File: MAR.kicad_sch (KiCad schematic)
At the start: 30 parts, among them J1 Conn_02x10_Odd_Even, J3 Conn_01x08_Pin, Q1 DMN3404, U1 74HC173, U3 74HC173

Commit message: increased resistor values for leds
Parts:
- R10, R11, R4, R5, R6, R7, R8, R9: value 200 -> 330; LCSC C25087 -> C25104
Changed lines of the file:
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@@
       (effects (font (size 1.27 1.27)) (justify left) hide)
     )
-    (property "Value" "200" (at 229.87 49.53 0)
+    (property "Value" "330" (at 229.87 49.53 0)
       (effects (font (size 1.27 1.27)) (justify left) hide)
     )
@@
       (effects (font (size 1.27 1.27)) hide)
     )
-    (property "LCSC" "C25087" (at 228.6 51.435 0)
+    (property "LCSC" "C25104" (at 228.6 51.435 0)
       (effects (font (size 1.27 1.27)) hide)
     )
@@
       (effects (font (size 1.27 1.27)) (justify left) hide)
     )
-    (property "Value" "200" (at 240.665 60.96 0)
+    (property "Value" "330" (at 240.665 60.96 0)
       (effects (font (size 1.27 1.27)) (justify left) hide)
     )
@@
       (effects (font (size 1.27 1.27)) hide)
     )
-    (property "LCSC" "C25087" (at 239.395 62.865 0)
+    (property "LCSC" "C25104" (at 239.395 62.865 0)
       (effects (font (size 1.27 1.27)) hide)
     )
@@
       (effects (font (size 1.27 1.27)) (justify left) hide)
     )
-    (property "Value" "200" (at 215.265 31.115 0)
+    (property "Value" "330" (at 215.265 31.115 0)
       (effects (font (size 1.27 1.27)) (justify left) hide)
     )
@@
       (effects (font (size 1.27 1.27)) hide)
     )
-    (property "LCSC" "C25087" (at 213.995 33.02 0)
+    (property "LCSC" "C25104" (at 213.995 33.02 0)
       (effects (font (size 1.27 1.27)) hide)
     )
@@
       (effects (font (size 1.27 1.27)) (justify left) hide)
     )
-    (property "Value" "200" (at 224.79 43.815 0)
+    (property "Value" "330" (at 224.79 43.815 0)
       (effects (font (size 1.27 1.27)) (justify left) hide)
     )
@@
       (effects (font (size 1.27 1.27)) hide)
     )
-    (property "LCSC" "C25087" (at 223.52 45.72 0)
+    (property "LCSC" "C25104" (at 223.52 45.72 0)
       (effects (font (size 1.27 1.27)) hide)
     )
@@
       (effects (font (size 1.27 1.27)) (justify left) hide)
     )
-    (property "Value" "200" (at 211.455 24.13 0)
+    (property "Value" "330" (at 211.455 24.13 0)
       (effects (font (size 1.27 1.27)) (justify left) hide)
     )
@@
       (effects (font (size 1.27 1.27)) hide)
     )
-    (property "LCSC" "C25087" (at 210.185 26.035 0)
+    (property "LCSC" "C25104" (at 210.185 26.035 0)
       (effects (font (size 1.27 1.27)) hide)
     )
@@
       (effects (font (size 1.27 1.27)) (justify left) hide)
     )
-    (property "Value" "200" (at 219.71 37.465 0)
+    (property "Value" "330" (at 219.71 37.465 0)
       (effects (font (size 1.27 1.27)) (justify left) hide)
     )
@@
       (effects (font (size 1.27 1.27)) hide)
     )
-    (property "LCSC" "C25087" (at 218.44 39.37 0)
+    (property "LCSC" "C25104" (at 218.44 39.37 0)
       (effects (font (size 1.27 1.27)) hide)
     )
@@
       (effects (font (size 1.27 1.27)) (justify left) hide)
     )
-    (property "Value" "200" (at 235.585 55.245 0)
+    (property "Value" "330" (at 235.585 55.245 0)
       (effects (font (size 1.27 1.27)) (justify left) hide)
     )
@@
       (effects (font (size 1.27 1.27)) hide)
     )
-    (property "LCSC" "C25087" (at 234.315 57.15 0)
+    (property "LCSC" "C25104" (at 234.315 57.15 0)
       (effects (font (size 1.27 1.27)) hide)
     )
@@
       (effects (font (size 1.27 1.27)) (justify left) hide)
     )
-    (property "Value" "200" (at 244.475 66.675 0)
+    (property "Value" "330" (at 244.475 66.675 0)
       (effects (font (size 1.27 1.27)) (justify left) hide)
     )
@@
       (effects (font (size 1.27 1.27)) hide)
     )
-    (property "LCSC" "C25087" (at 243.205 68.58 0)
-      (effects (font (size 1.27 1.27)) hide)
-    )
+    (property "LCSC" "C25104" (at 243.205 68.58 0)
+      (effects (font (size 1.27 1.27)) hide)
+    )

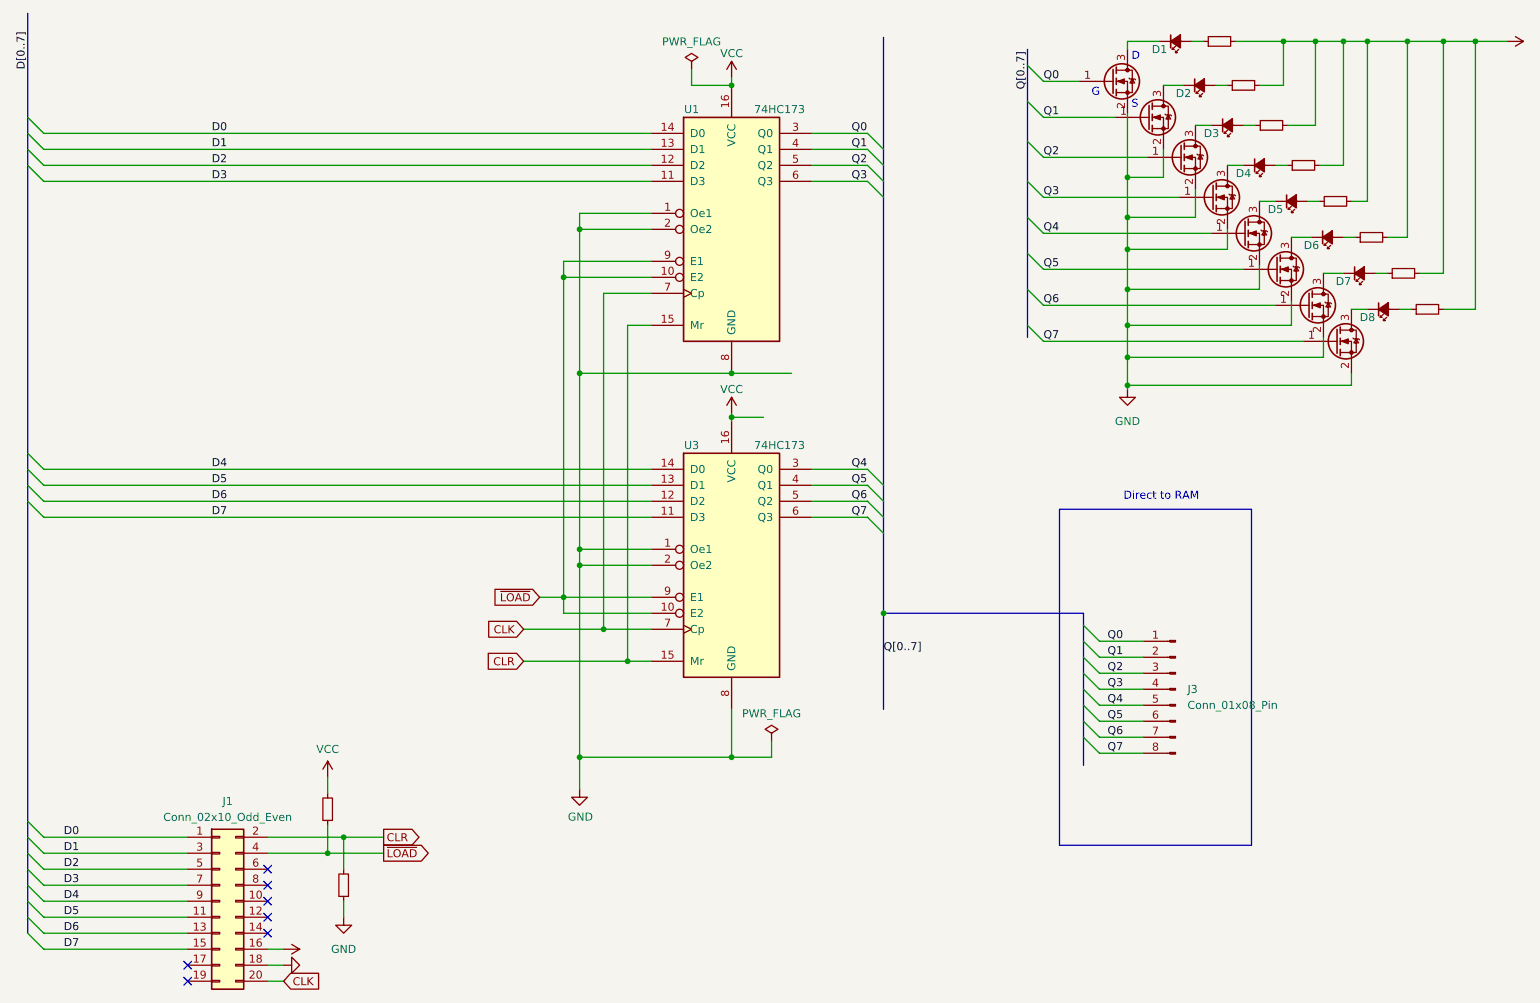
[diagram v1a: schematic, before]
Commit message: fixed grid alignment issue in schematic
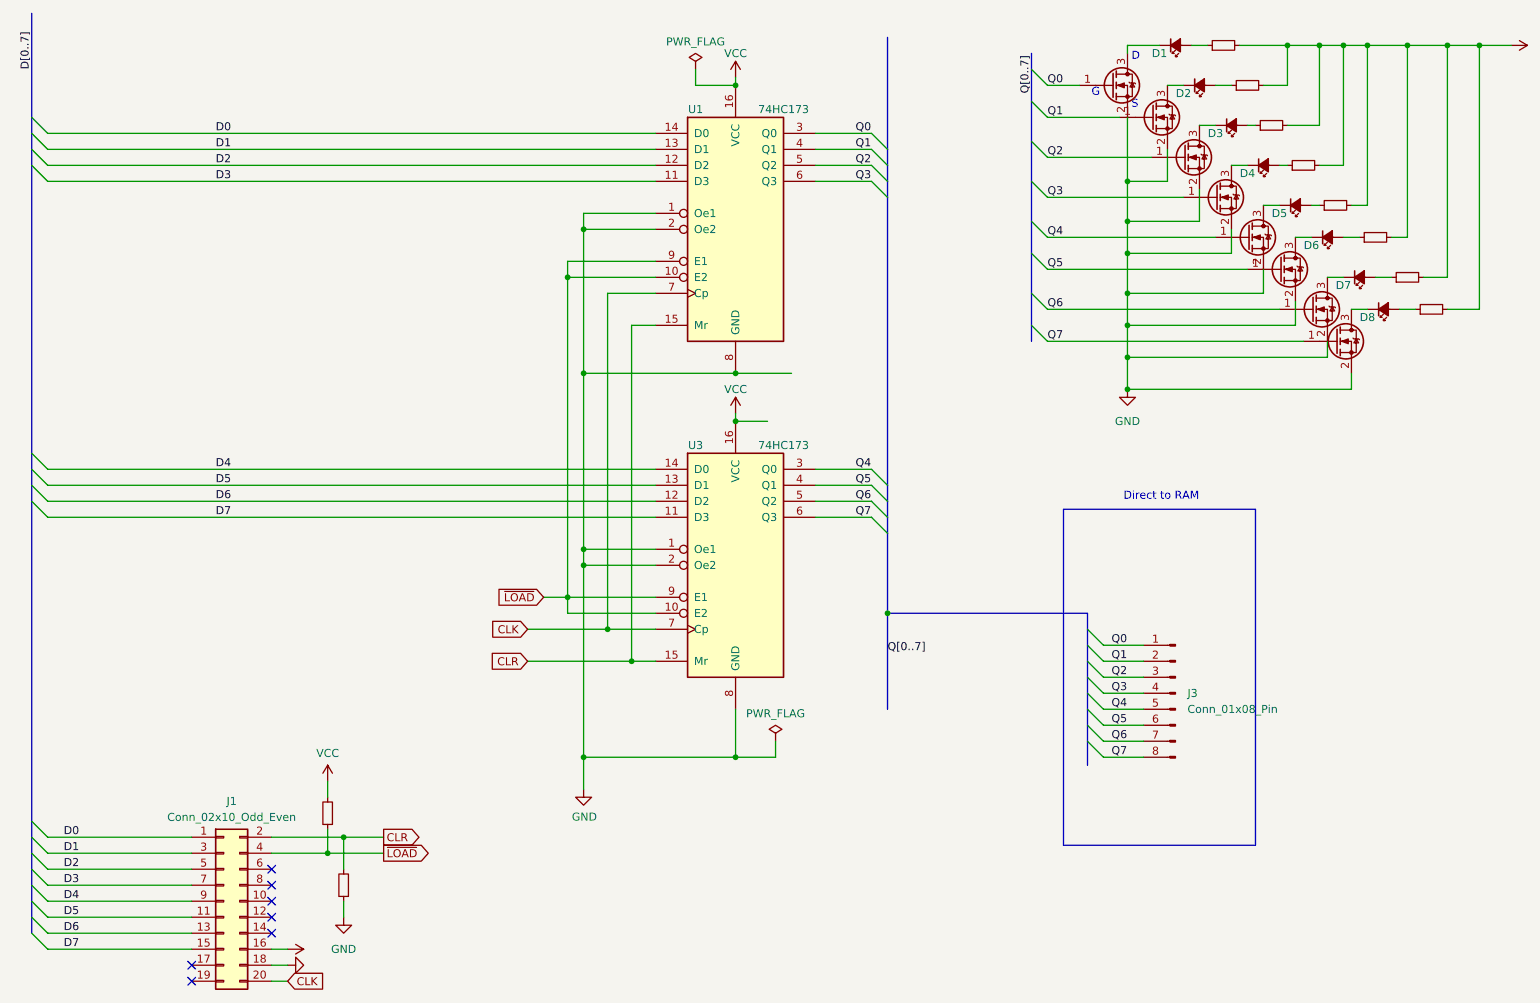
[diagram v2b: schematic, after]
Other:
- moved on the sheet: D1, D3, D4, D5, D7, J1, J3, U1, U3
